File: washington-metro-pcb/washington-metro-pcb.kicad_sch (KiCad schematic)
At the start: 301 parts, among them J1 Conn_01x04, U1 74AHC1G125

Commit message: WIP: resolving footprints
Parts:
- removed J1: Conn_01x04, Connector_PinHeader_2.54mm:PinHeader_1x04_P2.54mm_Vertical, symbol Connector_Generic:Conn_01x04
- removed LED1: WS2812B, vancouver-skytrain-pcb.pretty:XL-1010RGBC-WS2812B, symbol vancouver-skytrain-pcb:XL-1010RGBC-WS2812B
- added J2: Conn_01x12, Connector_PinHeader_2.54mm:PinHeader_1x12_P2.54mm_Vertical, symbol Connector_Generic:Conn_01x12
- added LED1: WS2812B, vancouver-skytrain-pcb.pretty:XL-1010RGBC-WS2812B, symbol washington-metro-pcb:XL-1010RGBC-WS2812B
- added R2 (x6): 0, R_0402_1005Metric, symbol jlcpcb-basic-resistor-0402:0
- C5: footprint vancouver-skytrain-pcb.pretty:C_0402_1005Metric -> C_0402_1005Metric
- LED1: symbol vancouver-skytrain-pcb:XL-1010RGBC-WS2812B -> washington-metro-pcb:XL-1010RGBC-WS2812B
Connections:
- net +5V: now also LED1.2 (VDD)
- net BLUE_LINE_IN: now also J2.10 (Pin_10), R2.2
- net BLUE_LINE_OUT: now also J2.9 (Pin_9), R2.1
- net GND: now also LED1.3 (VSS)
- net GREEN_LINE_IN: now also J2.4 (Pin_4), R2.2
- net GREEN_LINE_OUT: now also J2.3 (Pin_3), R2.1
- net LED_OUT: now also R2.2
- net ORANGE_LINE_IN: now also J2.6 (Pin_6), R2.2
- net ORANGE_LINE_OUT: now also J2.5 (Pin_5), R2.1
- net RED_LINE_IN: now also J2.8 (Pin_8), R2.2; no longer U1.4
- net RED_LINE_OUT: now also J2.7 (Pin_7), R2.1
- net SILVER_LINE_IN: now also U1.4, J2.12 (Pin_12)
- net SILVER_LINE_OUT: now also J2.11 (Pin_11), R2.1
- net YELLOW_LINE_IN: now also J2.2 (Pin_2), R2.2
- net YELLOW_LINE_OUT: now also J2.1 (Pin_1), R2.1
- net at LED1.4 (DIN): now also LED1.1 (DOUT)
- net at LED1.1 (DOUT): now also LED1.4 (DIN)
- no-connect marks 1 -> 0
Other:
- moved on the sheet: J1

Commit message: WIP: Silver line laid out
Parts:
- C5: footprint C_0402_1005Metric -> washington-metro-pcb:C_0402_1005Metric
- LED1: footprint vancouver-skytrain-pcb.pretty:XL-1010RGBC-WS2812B -> washington-metro-pcb:XL-1010RGBC-WS2812B
- R2: footprint R_0402_1005Metric -> Resistor_SMD:R_0402_1005Metric

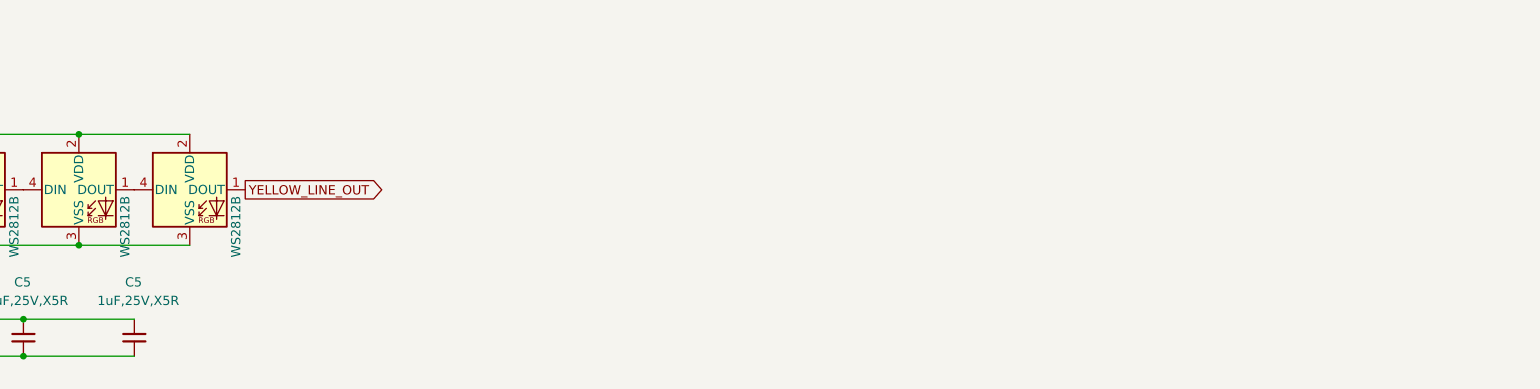
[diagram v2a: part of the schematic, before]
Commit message: Most of the stations LEDs and tracks laid out
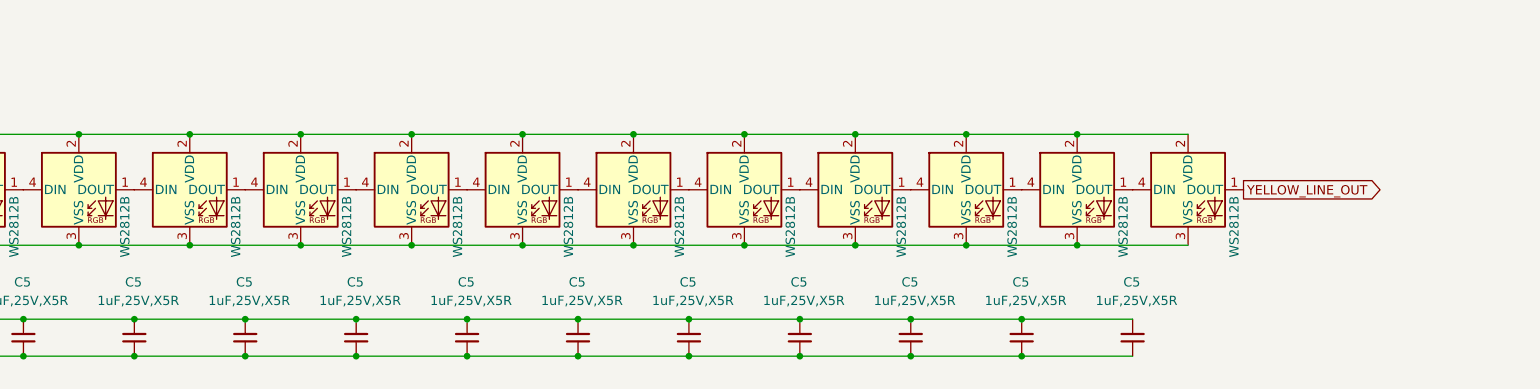
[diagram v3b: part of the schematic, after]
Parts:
- added C5 (x9): 1uF,25V,X5R, C_0402_1005Metric, symbol jlcpcb-basic-capacitor-0402:1uF,25V,X5R
- added LED1 (x9): WS2812B, washington-metro-pcb:XL-1010RGBC-WS2812B, symbol washington-metro-pcb:XL-1010RGBC-WS2812B
- C5: footprint washington-metro-pcb:C_0402_1005Metric -> C_0402_1005Metric
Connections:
- net +5V: now also C5.1, C5.1, C5.1, C5.1, C5.1, C5.1, C5.1, C5.1, C5.1, LED1.2 (VDD), LED1.2 (VDD), LED1.2 (VDD), LED1.2 (VDD), LED1.2 (VDD), LED1.2 (VDD), LED1.2 (VDD), LED1.2 (VDD), LED1.2 (VDD)
- net GND: now also C5.2, C5.2, C5.2, C5.2, C5.2, C5.2, C5.2, C5.2, C5.2, LED1.3 (VSS), LED1.3 (VSS), LED1.3 (VSS), LED1.3 (VSS), LED1.3 (VSS), LED1.3 (VSS), LED1.3 (VSS), LED1.3 (VSS), LED1.3 (VSS)
- net YELLOW_LINE_OUT: now also LED1.1 (DOUT); no longer LED1.1 (DOUT)
- new net: LED1.1 (DOUT), LED1.4 (DIN) (x9)

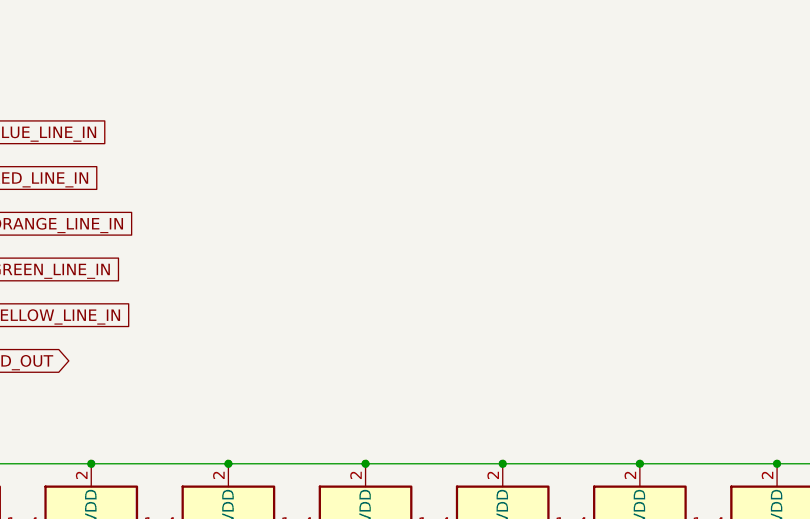
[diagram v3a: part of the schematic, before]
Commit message: Added mounting holes and version information
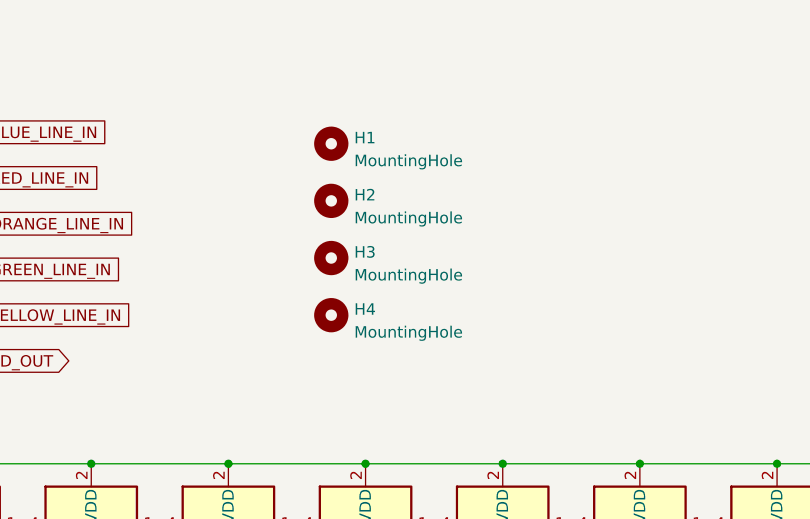
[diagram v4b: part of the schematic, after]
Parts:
- added H1, H2, H3, H4: MountingHole, MountingHole:MountingHole_3.2mm_M3, symbol Mechanical:MountingHole
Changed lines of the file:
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@@
     )
   )
+  (symbol (lib_id "Mechanical:MountingHole") (at 204.47 27.94 0) (unit 1)
+    (in_bom yes) (on_board yes) (dnp no) (fields_autoplaced)
+    (property "Reference" "H1" (at 207.01 27.305 0)
+      (effects (font (size 1.27 1.27)) (justify left))
+    )
+    (property "Value" "MountingHole" (at 207.01 29.845 0)
+      (effects (font (size 1.27 1.27)) (justify left))
+    )
+    (property "Footprint" "MountingHole:MountingHole_3.2mm_M3" (at 204.47 27.94 0)
+      (effects (font (size 1.27 1.27)) hide)
+    )
+    (property "Datasheet" "~" (at 204.47 27.94 0)
+      (effects (font (size 1.27 1.27)) hide)
+    )
+    (instances
+      (project "washington-metro-pcb"
+        (path "/3ce3292e-040e-4421-8852-165c6a913283"
+          (reference "H1") (unit 1)
+        )
+      )
+    )
+  )
   (symbol (lib_id "jlcpcb-basic-capacitor-0402:1uF,25V,X5R ") (at 33.02 293.37 0) (unit 1)
     (in_bom yes) (on_board yes) (dnp no)
@@
     )
   )
+  (symbol (lib_id "Mechanical:MountingHole") (at 204.47 34.29 0) (unit 1)
+    (in_bom yes) (on_board yes) (dnp no) (fields_autoplaced)
+    (property "Reference" "H2" (at 207.01 33.655 0)
+      (effects (font (size 1.27 1.27)) (justify left))
+    )
+    (property "Value" "MountingHole" (at 207.01 36.195 0)
+      (effects (font (size 1.27 1.27)) (justify left))
+    )
+    (property "Footprint" "MountingHole:MountingHole_3.2mm_M3" (at 204.47 34.29 0)
+      (effects (font (size 1.27 1.27)) hide)
+    )
+    (property "Datasheet" "~" (at 204.47 34.29 0)
+      (effects (font (size 1.27 1.27)) hide)
+    )
+    (instances
+      (project "washington-metro-pcb"
+        (path "/3ce3292e-040e-4421-8852-165c6a913283"
+          (reference "H2") (unit 1)
+        )
+      )
+    )
+  )
   (symbol (lib_id "jlcpcb-basic-capacitor-0402:1uF,25V,X5R ") (at 259.08 344.17 0) (unit 1)
     (in_bom yes) (on_board yes) (dnp no)
@@
     )
   )
+  (symbol (lib_id "Mechanical:MountingHole") (at 204.47 40.64 0) (unit 1)
+    (in_bom yes) (on_board yes) (dnp no) (fields_autoplaced)
+    (property "Reference" "H3" (at 207.01 40.005 0)
+      (effects (font (size 1.27 1.27)) (justify left))
+    )
+    (property "Value" "MountingHole" (at 207.01 42.545 0)
+      (effects (font (size 1.27 1.27)) (justify left))
+    )
+    (property "Footprint" "MountingHole:MountingHole_3.2mm_M3" (at 204.47 40.64 0)
+      (effects (font (size 1.27 1.27)) hide)
+    )
+    (property "Datasheet" "~" (at 204.47 40.64 0)
+      (effects (font (size 1.27 1.27)) hide)
+    )
+    (instances
+      (project "washington-metro-pcb"
+        (path "/3ce3292e-040e-4421-8852-165c6a913283"
+          (reference "H3") (unit 1)
+        )
+      )
+    )
+  )
   (symbol (lib_id "washington-metro-pcb:XL-1010RGBC-WS2812B") (at 39.37 222.25 0) (unit 1)
     (in_bom yes) (on_board yes) (dnp no)
@@
         )
       )
+    )
+  )
+  (symbol (lib_id "Mechanical:MountingHole") (at 204.47 46.99 0) (unit 1)
+    (in_bom yes) (on_board yes) (dnp no) (fields_autoplaced)
+    (property "Reference" "H4" (at 207.01 46.355 0)
+      (effects (font (size 1.27 1.27)) (justify left))
+    )
+    (property "Value" "MountingHole" (at 207.01 48.895 0)
+      (effects (font (size 1.27 1.27)) (justify left))
+    )
+    (property "Footprint" "MountingHole:MountingHole_3.2mm_M3" (at 204.47 46.99 0)
+      (effects (font (size 1.27 1.27)) hide)
+    )
+    (property "Datasheet" "~" (at 204.47 46.99 0)
+      (effects (font (size 1.27 1.27)) hide)
+    )
+    (instances
+      (project "washington-metro-pcb"
+        (path "/3ce3292e-040e-4421-8852-165c6a913283"
+          (reference "H4") (unit 1)
+        )
+      )
